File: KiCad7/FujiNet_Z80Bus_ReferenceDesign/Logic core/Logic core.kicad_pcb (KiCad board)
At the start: 2 copper layers, 100 x 135.9 mm, 24 parts, among them IC1 7404N, IC10 7408N, IC2 7432N, IC3 7474N, IC4 7432N, IC5 7408N, IC6 7432N, IC7 7432N, IC8 7432N, IC9 7408N, J1 Logic core connector, Q1 2N2222 (BC337)

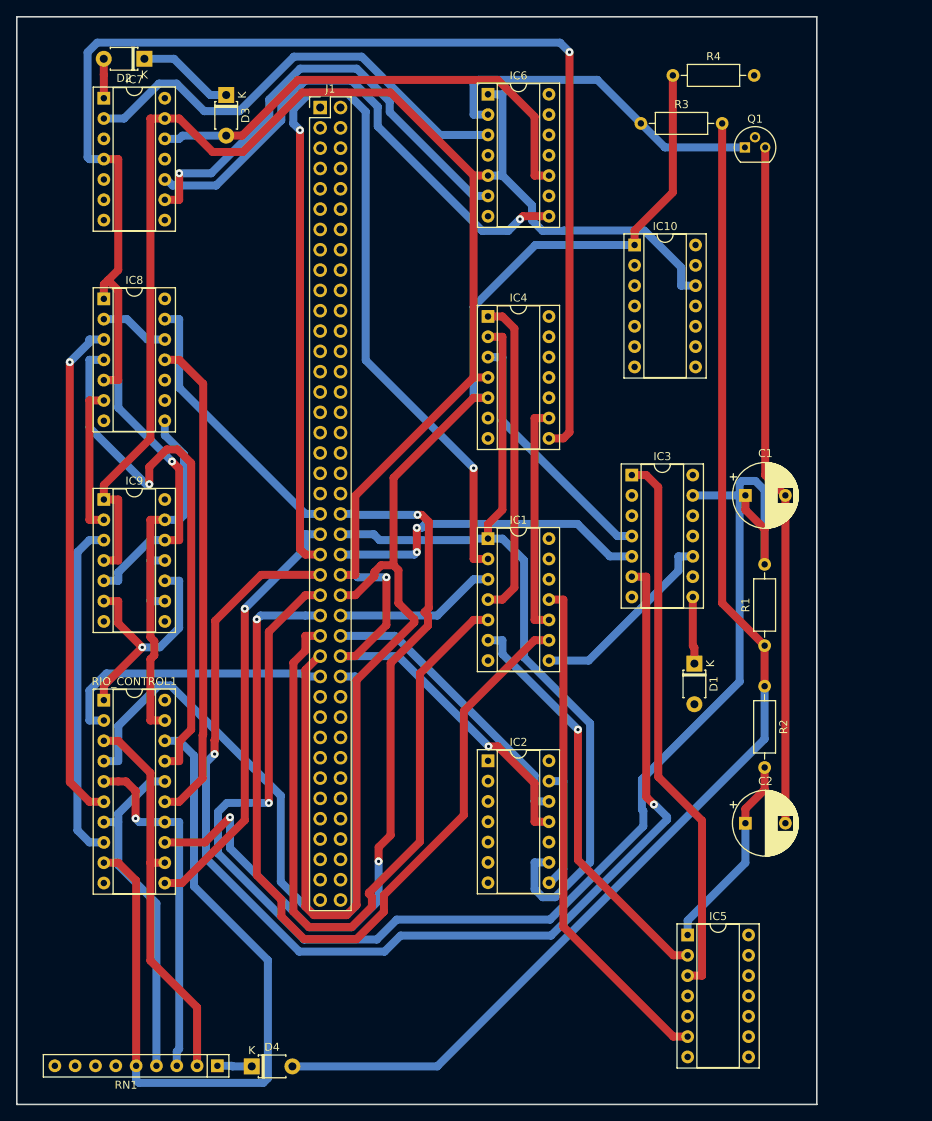
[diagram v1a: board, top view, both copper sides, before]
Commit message: KiCad experiment with logic core PCB
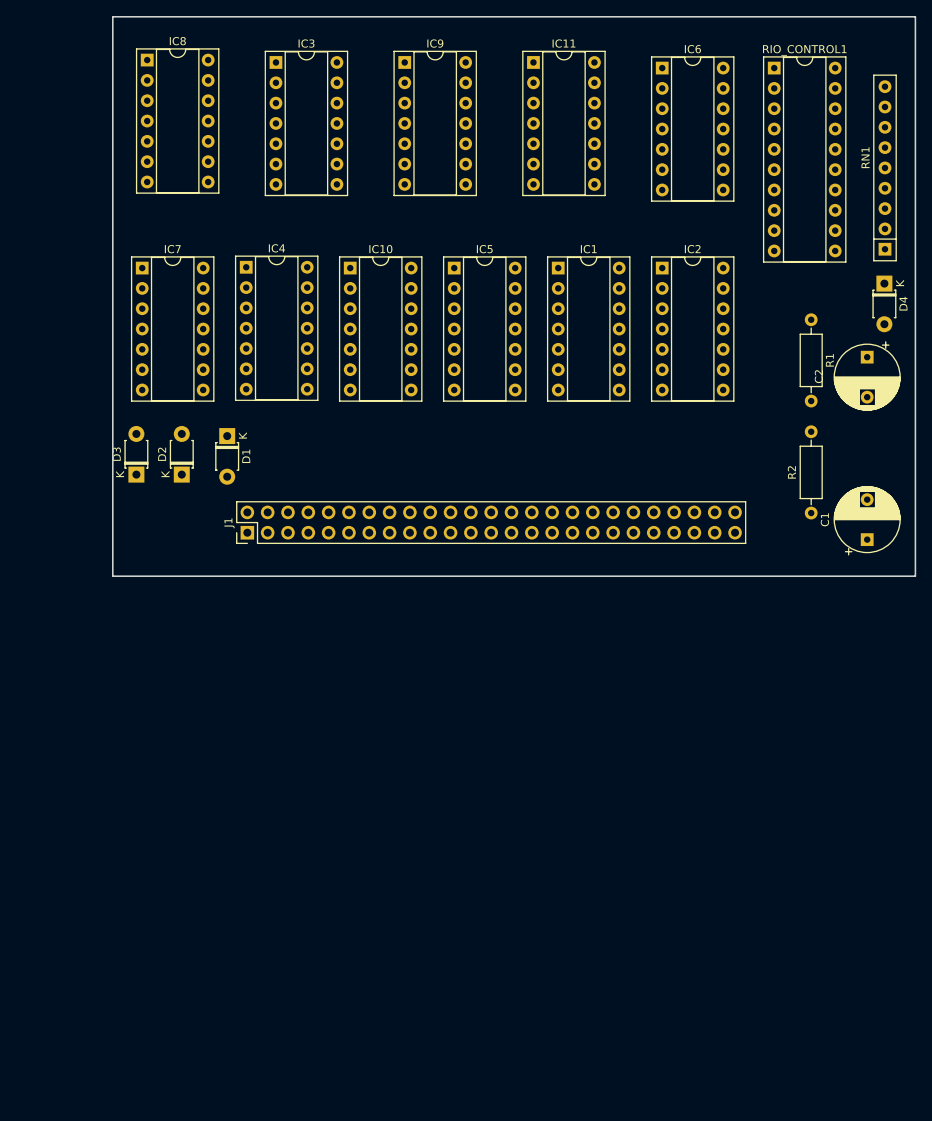
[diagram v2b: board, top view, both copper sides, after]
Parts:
- removed Q1: 2N2222 (BC337), Package_TO_SOT_THT:TO-92
- removed R3, R4: 1K, Resistor_THT:R_Axial_DIN0207_L6.3mm_D2.5mm_P10.16mm_Horizontal
- added IC11: 74HC08N, Package_DIP:DIP-14_W7.62mm_Socket, F.Cu at (114.3, 54.8)
- IC10: value 7408N -> 74HC08N
- IC2, IC7, IC8: value 7432N -> 74HC32N
- IC3: value 7474N -> 74HC32N
- IC4: value 7432N -> 7474N
- IC5, IC9: value 7408N -> 74HC32N
- IC6: value 7432N -> 74HC08N
- J1: footprint Connector_PinHeader_2.54mm:PinHeader_2x40_P2.54mm_Vertical -> Connector_PinHeader_2.54mm:PinHeader_2x25_P2.54mm_Vertical
- moved RN1 131.8 mm to (158.2, 78.1), turned to 90 degrees
- moved D4 125.8 mm to (158.2, 82.4), turned to -90 degrees
- moved RIO_CONTROL1 115.2 mm to (144.4, 55.5)
- moved IC5 88.3 mm to (104.4, 80.5)
- moved IC3 68.1 mm to (82.1, 54.8)
- moved IC9 66.3 mm to (98.2, 54.8)
- moved IC2 65.3 mm to (130.4, 80.5)
- moved D1 65.0 mm to (76.0, 101.5)
- moved C2 60.2 mm to (156.0, 91.6), turned to -90 degrees
- moved J1 53.9 mm to (78.5, 113.5), turned to 90 degrees
- moved D2 52.2 mm to (70.3, 106.3), turned to 90 degrees
- moved D3 48.8 mm to (64.7, 106.3), turned to 90 degrees
- moved R1 41.1 mm to (149.0, 86.9), turned to -90 degrees
- moved IC10 35.7 mm to (91.4, 80.5)
- moved IC1 34.9 mm to (117.4, 80.5)
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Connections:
- net /Logic core connectors/ESP_CONTROL.BUSRQ renamed /Logic core connectors2/Z80_BUS_CONTROL.Z80_ADD_OE
- net /Logic core connectors/ESP_CONTROL.NMI renamed /Logic core connectors2/Z80_BUS_CONTROL.Z80_DATA_OE
- net /Logic core connectors/ESP_CONTROL.ROMCS renamed /Logic core connectors2/Z80_BUS_CONTROL.Z80_DATA_DIR
- net /Logic core connectors/ESP_CONTROL.WAIT renamed /Logic core connectors2/Z80_BUS_CONTROL.Z80_ADD_DIR
- net /Logic core connectors/LOCAL_CONTROL.IORQ renamed /Logic core connectors2/CACHE_CONTROL.WE
- net /Logic core connectors/LOCAL_CONTROL.MEMRQ renamed /Logic core connectors2/CACHE_CONTROL.OE
- net /Logic core connectors/LOCAL_CONTROL.RD renamed /Logic core connectors2/CACHE_CONTROL.DATASTATUS+PERM_Z80_IORQ
- net /Logic core connectors/LOCAL_CONTROL.WR renamed /Logic core connectors2/CACHE_CONTROL.A16
- net /Logic core connectors/Z80_BUS_CONTROL.Z80_ADD_OE renamed /Logic core connectors2/CACHE_CONTROL.CS
- C2 pad 1: Net-(IC5A-I0) -> Net-(C2-Pad1)
- D2 pad 1: /Z80 BUS CONTROL/Z80_CONTROL.BUSRQ -> /Z80_CONTROL.BUSRQ
- D3 pad 1: /Z80 BUS CONTROL/Z80_CONTROL.BUSRQ -> /Z80_CONTROL.BUSRQ
- IC1 pad 10: Net-(IC1E-O) -> Net-(IC1-Pad10)
- IC1 pad 11: Net-(IC1E-I) -> Net-(IC1-Pad11)
- IC1 pad 14: (no net) -> unconnected-(IC1G-VCC-Pad14)
- IC1 pad 4: Net-(IC1B-O) -> Net-(IC1-Pad4)
- IC1 pad 6: Net-(IC1C-O) -> Net-(IC1-Pad6)
- IC1 pad 7: (no net) -> unconnected-(IC1G-GND-Pad7)
- IC1 pad 8: Net-(IC1D-O) -> Net-(IC4B-~{S})
- IC10 pad 1: /CACHE_DATASTATUS -> /PERM_Z80_IORQ
- IC10 pad 10: /CACHE CONTROL/LOCAL_CONTROL.RD -> /RIO CONTROL/RIO_CONTROL.A16
- IC10 pad 11: /CACHE CONTROL/CACHE_CONTROL.CS -> Net-(IC10-Pad11)
- IC10 pad 12: /PERM_Z80_IORQ -> /ESP_IOD_CONFIG
- IC10 pad 13: /CACHE CONTROL/LOCAL_CONTROL.MEMRQ -> /RIO CONTROL/RIO_CONTROL.ROM_RDY
- IC10 pad 2: /CACHE CONTROL/LOCAL_CONTROL.IORQ -> Net-(IC10-Pad2)
- IC10 pad 3: /CACHE CONTROL/CACHE_CONTROL.A16 -> /RIO CONTROL/Z80_RD+ESP_IOD_CONFIG+PERM_Z80_IORQ
- IC10 pad 4: /CACHE CONTROL/Z80_CONTROL.WR -> /PERM_Z80_IORQ
- IC10 pad 5: /CACHE CONTROL/LOCAL_CONTROL.WR -> /ESP_IOD_CONFIG
- IC10 pad 6: /CACHE CONTROL/CACHE_CONTROL.WE -> /RIO CONTROL/RIO_CONTROL.A16
- IC10 pad 8: /CACHE CONTROL/CACHE_CONTROL.OE -> /RIO CONTROL/RIO_CONTROL.CE
- IC10 pad 9: /CACHE CONTROL/Z80_CONTROL.RD -> Net-(IC10-Pad11)
- IC2 pad 10: /Z80_CONTROL.IORQ -> (no net)
- IC2 pad 11: /PERM_Z80_IORQ -> (no net)
- IC2 pad 12: /IORQ_FILTER_BIT -> (no net)
- IC2 pad 13: Net-(IC2C-O) -> (no net)
- IC2 pad 14: (no net) -> GND
- IC2 pad 7: (no net) -> +5V
- IC2 pad 8: Net-(IC2C-O) -> (no net)
- IC2 pad 9: /ESP_HARDLOCK -> (no net)
- IC3 pad 1: /CLR_Z80_HARDLOCK -> (no net)
- IC3 pad 10: Net-(IC1D-O) -> /Z80_CONTROL.IORQ
- IC3 pad 11: unconnected-(IC3B-CLK-Pad11) -> /PERM_Z80_IORQ
- IC3 pad 12: unconnected-(IC3B-D-Pad12) -> /IORQ_FILTER_BIT
- IC3 pad 13: /ESP_WAIT_RESET -> Net-(IC3-Pad13)
- IC3 pad 2: unconnected-(IC3A-D-Pad2) -> (no net)
- IC3 pad 3: unconnected-(IC3A-CLK-Pad3) -> (no net)
- IC3 pad 4: /PRE_Z80_HARDLOCK -> (no net)
- IC3 pad 5: /Z80_HARDLOCK -> (no net)
- IC3 pad 6: /!Z80_HARDLOCK -> (no net)
- IC3 pad 8: Net-(D1-K) -> Net-(IC3-Pad13)
- IC3 pad 9: unconnected-(IC3B-Q-Pad9) -> /ESP_HARDLOCK
- IC4 pad 1: Net-(IC1B-O) -> /CLR_Z80_HARDLOCK
- IC4 pad 10: /RIO CONTROL/ESP_CONTROL.BUSRQ -> Net-(IC4B-~{S})
- IC4 pad 11: (no net) -> unconnected-(IC4B-C-Pad11)
- IC4 pad 12: (no net) -> unconnected-(IC4B-D-Pad12)
- IC4 pad 13: (no net) -> /ESP_WAIT_RESET
- IC4 pad 2: /ESP_HARDLOCK -> unconnected-(IC4A-D-Pad2)
- IC4 pad 3: /PRE_Z80_HARDLOCK -> unconnected-(IC4A-C-Pad3)
- IC4 pad 4: /PERM_Z80_IORQ -> /PRE_Z80_HARDLOCK
- IC4 pad 5: /CACHE_DATASTATUS -> /Z80_HARDLOCK
- IC4 pad 6: /CACHE CONTROL/CACHE_CONTROL.DATASTATUS+PERM_Z80_IORQ -> /!Z80_HARDLOCK
- IC4 pad 8: /ESP_IOD_CONFIG -> Net-(D1-K)
- IC4 pad 9: Net-(IC1E-O) -> unconnected-(IC4B-Q-Pad9)
- IC5 pad 1: Net-(IC5A-I0) -> Net-(IC1-Pad4)
- IC5 pad 10: (no net) -> /ESP_CONTROL.BUSRQ
- IC5 pad 2: Net-(IC1C-O) -> /ESP_HARDLOCK
- IC5 pad 3: /CLR_Z80_HARDLOCK -> /PRE_Z80_HARDLOCK
- IC5 pad 4: /RIO CONTROL/ESP_CONTROL.MEMRQ -> /PERM_Z80_IORQ
- IC5 pad 5: /RIO CONTROL/ESP_CONTROL.IORQ -> /CACHE_DATASTATUS
- IC5 pad 6: Net-(IC1E-I) -> /CACHE CONTROL/CACHE_CONTROL.DATASTATUS+PERM_Z80_IORQ
- IC5 pad 8: (no net) -> /ESP_IOD_CONFIG
- IC5 pad 9: (no net) -> Net-(IC1-Pad10)
- IC6 pad 1: /PERM_Z80_IORQ -> Net-(C2-Pad1)
- IC6 pad 10: /Z80 BUS CONTROL/Z80_DATA_CONNECT -> (no net)
- IC6 pad 2: /Z80 BUS CONTROL/!CACHE_DATASTATUS -> Net-(IC1-Pad6)
- IC6 pad 3: Net-(IC6A-O) -> /CLR_Z80_HARDLOCK
- IC6 pad 4: /Z80 BUS CONTROL/Z80_CONTROL.RD -> /ESP_CONTROL.MEMRQ
- IC6 pad 5: /PERM_Z80_IORQ -> /ESP_CONTROL.IORQ
- IC6 pad 6: Net-(IC6B-O) -> Net-(IC1-Pad11)
- IC6 pad 8: Net-(IC6C-O) -> (no net)
- IC6 pad 9: /Z80 BUS CONTROL/ESP_CONTROL.WR -> (no net)
- IC7 pad 1: /Z80 BUS CONTROL/Z80_ADD_CONNECT -> /PERM_Z80_IORQ
- IC7 pad 10: Net-(IC6C-O) -> /Z80 BUS CONTROL/Z80_DATA_CONNECT
- IC7 pad 11: /Z80 BUS CONTROL/Z80_BUS_CONTROL.Z80_DATA_OE -> (no net)
- IC7 pad 12: /Z80 BUS CONTROL/Z80_DATA_CONNECT -> (no net)
- IC7 pad 13: /PERM_Z80_IORQ -> (no net)
- IC7 pad 2: Net-(IC6A-O) -> /Z80 BUS CONTROL/!CACHE_DATASTATUS
- IC7 pad 3: /Z80 BUS CONTROL/Z80_BUS_CONTROL.Z80_ADD_OE -> Net-(IC7-Pad3)
- IC7 pad 4: /ESP_IOD_CONFIG -> /Z80_CONTROL.RD
- IC7 pad 5: /Z80 BUS CONTROL/ESP_CONTROL.MEMRQ -> /PERM_Z80_IORQ
- IC7 pad 6: /Z80 BUS CONTROL/Z80_BUS_CONTROL.Z80_ADD_DIR -> Net-(IC7-Pad6)
- IC7 pad 8: /Z80 BUS CONTROL/Z80_BUS_CONTROL.Z80_DATA_DIR -> Net-(IC7-Pad8)
- IC7 pad 9: Net-(IC6B-O) -> /ESP_CONTROL.WR
- IC8 pad 1: /ESP_IOD_CONFIG -> /Z80 BUS CONTROL/Z80_ADD_CONNECT
- IC8 pad 10: /RIO CONTROL/Z80_CONTROL.MEMRQ -> Net-(IC7-Pad8)
- IC8 pad 11: /RIO CONTROL/ROM_WR_PROTECT+Z80_WR -> /Z80 BUS CONTROL/Z80_BUS_CONTROL.Z80_DATA_OE
- IC8 pad 12: /RIO CONTROL/Z80_CONTROL.WR -> /Z80 BUS CONTROL/Z80_DATA_CONNECT
- IC8 pad 13: /ESP_ROM_WR_PROTECT -> /PERM_Z80_IORQ
- IC8 pad 2: /RIO CONTROL/Z80_CONTROL.WR -> Net-(IC7-Pad3)
- IC8 pad 3: /RIO CONTROL/Z80_WR+ESP_IOD_CONFIG -> /Z80 BUS CONTROL/Z80_BUS_CONTROL.Z80_ADD_OE
- IC8 pad 4: /RIO CONTROL/Z80_CONTROL.RD -> /ESP_IOD_CONFIG
- IC8 pad 5: /ESP_IOD_CONFIG -> /ESP_CONTROL.MEMRQ
- IC8 pad 6: Net-(IC8B-O) -> /Z80 BUS CONTROL/Z80_BUS_CONTROL.Z80_ADD_DIR
- IC8 pad 8: /RIO CONTROL/RIO_CONTROL.ROM_RDY -> /Z80 BUS CONTROL/Z80_BUS_CONTROL.Z80_DATA_DIR
- IC8 pad 9: /RIO CONTROL/ESP_CONTROL.ROMCS -> Net-(IC7-Pad6)
- IC9 pad 1: /PERM_Z80_IORQ -> /ESP_IOD_CONFIG
- IC9 pad 10: /RIO CONTROL/RIO_CONTROL.A16 -> /Z80_CONTROL.MEMRQ
- IC9 pad 11: Net-(IC9C-I0) -> /RIO CONTROL/ROM_WR_PROTECT+Z80_WR
- IC9 pad 12: /ESP_IOD_CONFIG -> /Z80_CONTROL.WR
- IC9 pad 13: /RIO CONTROL/RIO_CONTROL.ROM_RDY -> /ESP_ROM_WR_PROTECT
- IC9 pad 2: Net-(IC8B-O) -> /Z80_CONTROL.WR
- IC9 pad 3: /RIO CONTROL/Z80_RD+ESP_IOD_CONFIG+PERM_Z80_IORQ -> /RIO CONTROL/Z80_WR+ESP_IOD_CONFIG
- IC9 pad 4: /PERM_Z80_IORQ -> /Z80_CONTROL.RD
- IC9 pad 6: /RIO CONTROL/RIO_CONTROL.A16 -> Net-(IC10-Pad2)
- IC9 pad 8: /RIO CONTROL/RIO_CONTROL.CE -> /RIO CONTROL/RIO_CONTROL.ROM_RDY
- IC9 pad 9: Net-(IC9C-I0) -> /ESP_CONTROL.ROMCS
- J1 pad 1: /Logic core connectors/Z80_CONTROL.RD -> /Z80_CONTROL.RD
- J1 pad 10: /Logic core connectors/Z80_CONTROL.RESET -> /ESP_CONTROL.ROMCS
- J1 pad 11: /Logic core connectors/ESP_CONTROL.RD -> /LOCAL_CONTROL.RD
- J1 pad 12: /Logic core connectors/ESP_CONTROL.WR -> /LOCAL_CONTROL.WR
- J1 pad 13: /Logic core connectors/ESP_CONTROL.IORQ -> /LOCAL_CONTROL.IORQ
- J1 pad 14: /Logic core connectors/ESP_CONTROL.MEMRQ -> /LOCAL_CONTROL.MEMRQ
- J1 pad 2: /Logic core connectors/Z80_CONTROL.WR -> /Z80_CONTROL.WR
- J1 pad 24: /Logic core connectors/Z80_BUS_CONTROL.Z80_ADD_DIR -> unconnected-(J1-Pin_24-Pad24)
- J1 pad 25: /Logic core connectors/Z80_BUS_CONTROL.Z80_DATA_DIR -> unconnected-(J1-Pin_25-Pad25)
- J1 pad 26: /Logic core connectors/Z80_BUS_CONTROL.Z80_DATA_OE -> /ESP_ROM_WR_PROTECT
- J1 pad 27: /Logic core connectors/CACHE_CONTROL.DATASTATUS+PERM_Z80_IORQ -> /ESP_ROMSEL_0
- J1 pad 28: /Logic core connectors/CACHE_CONTROL.A16 -> /ESP_ROMSEL_1
- J1 pad 29: /Logic core connectors/CACHE_CONTROL.WE -> /ESP_HARDLOCK
- J1 pad 3: /Logic core connectors/Z80_CONTROL.IORQ -> /Z80_CONTROL.MEMRQ
- J1 pad 30: /Logic core connectors/CACHE_CONTROL.OE -> /!ESP_HARDLOCK
- J1 pad 31: /Logic core connectors/CACHE_CONTROL.CS -> /Z80_HARDLOCK
- J1 pad 32: /Logic core connectors/RIO_CONTROL.A14 -> /!Z80_HARDLOCK
- J1 pad 33: /Logic core connectors/RIO_CONTROL.A15 -> /PERM_Z80_IORQ
- J1 pad 34: /Logic core connectors/RIO_CONTROL.WE -> /ESP_WAIT_RESET
- J1 pad 35: /Logic core connectors/RIO_CONTROL.OE -> /CACHE_DATASTATUS
- J1 pad 36: unconnected-(J1-Pin_36-Pad36) -> /WAIT_IO
- J1 pad 37: unconnected-(J1-Pin_37-Pad37) -> /Z80_HARDLOCK_SET
- J1 pad 38: unconnected-(J1-Pin_38-Pad38) -> /Z80_HARDLOCK_RESET
- J1 pad 39: unconnected-(J1-Pin_39-Pad39) -> /IORQ_FILTER_BIT
- J1 pad 4: /Logic core connectors/Z80_CONTROL.MEMRQ -> /Z80_CONTROL.BUSRQ
- J1 pad 40: unconnected-(J1-Pin_40-Pad40) -> /Z80_A15
- J1 pad 41: /ESP_ROM_WR_PROTECT -> /Z80_A14
- J1 pad 42: /ESP_ROMSEL_0 -> /Logic core connectors2/RIO_CONTROL.A14
- J1 pad 43: /ESP_ROMSEL_1 -> /Logic core connectors2/RIO_CONTROL.A15
- J1 pad 44: /ESP_HARDLOCK -> /Logic core connectors2/RIO_CONTROL.WE
- J1 pad 45: /!ESP_HARDLOCK -> /Logic core connectors2/RIO_CONTROL.OE
- J1 pad 46: /Z80_HARDLOCK -> +5V
- J1 pad 47: /!Z80_HARDLOCK -> GND
- J1 pad 48: /PERM_Z80_IORQ -> unconnected-(J1-Pin_48-Pad48)
- J1 pad 49: /ESP_WAIT_RESET -> unconnected-(J1-Pin_49-Pad49)
- J1 pad 5: /Logic core connectors/Z80_CONTROL.BUSRQ -> /Z80_CONTROL.WAIT
- J1 pad 50: /CACHE_DATASTATUS -> unconnected-(J1-Pin_50-Pad50)
- J1 pad 6: /Logic core connectors/Z80_CONTROL.WAIT -> /ESP_CONTROL.WR
- J1 pad 7: /Logic core connectors/Z80_CONTROL.NMI -> /ESP_CONTROL.IORQ
- J1 pad 8: /Logic core connectors/Z80_CONTROL.ROMCS -> /ESP_CONTROL.MEMRQ
- J1 pad 9: /Logic core connectors/Z80_CONTROL.BUSACK -> /ESP_CONTROL.BUSRQ
- R2 pad 2: Net-(IC5A-I0) -> Net-(C2-Pad1)
- RIO_CONTROL1 pad 17: /RIO CONTROL/Z80_CONTROL.RD -> /Z80_CONTROL.RD
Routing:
- net /PERM_Z80_IORQ: track 275.0 -> 0.00 mm, vias 2 -> 0
- net /ESP_IOD_CONFIG: track 198.8 -> 0.00 mm, vias 2 -> 0
- net /ESP_WAIT_RESET: track 182.4 -> 0.00 mm, vias 1 -> 0
- net /CACHE_DATASTATUS: track 181.1 -> 0.00 mm
- net +5V: track 155.1 -> 0.00 mm
- net /!Z80_HARDLOCK: track 148.3 -> 0.00 mm, vias 2 -> 0
- net /!ESP_HARDLOCK: track 132.3 -> 0.00 mm, vias 2 -> 0
- net /ESP_HARDLOCK: track 107.7 -> 0.00 mm
- net /WAIT_IO: track 105.5 -> 0.00 mm, vias 1 -> 0
- net /ESP_ROMSEL_0: track 99.1 -> 0.00 mm, vias 3 -> 0
- net /RIO CONTROL/RIO_CONTROL.A14: track 95.3 -> 0.00 mm
- net /Z80_HARDLOCK_RESET: track 91.9 -> 0.00 mm
- net /Z80_A14: track 87.2 -> 0.00 mm
- net GND: track 85.5 -> 0.00 mm
- net /RIO CONTROL/Z80_CONTROL.RD: track 69.4 -> 0.00 mm, vias 1 -> 0
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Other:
- board size 100 x 135.9 mm -> 100.3 x 69.9 mm
